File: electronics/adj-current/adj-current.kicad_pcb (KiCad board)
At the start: 2 copper layers, 9 parts, among them J1 Power, J2 Output, Q1 IRLZ44N, U1 LM358, U2 TL431DBZ

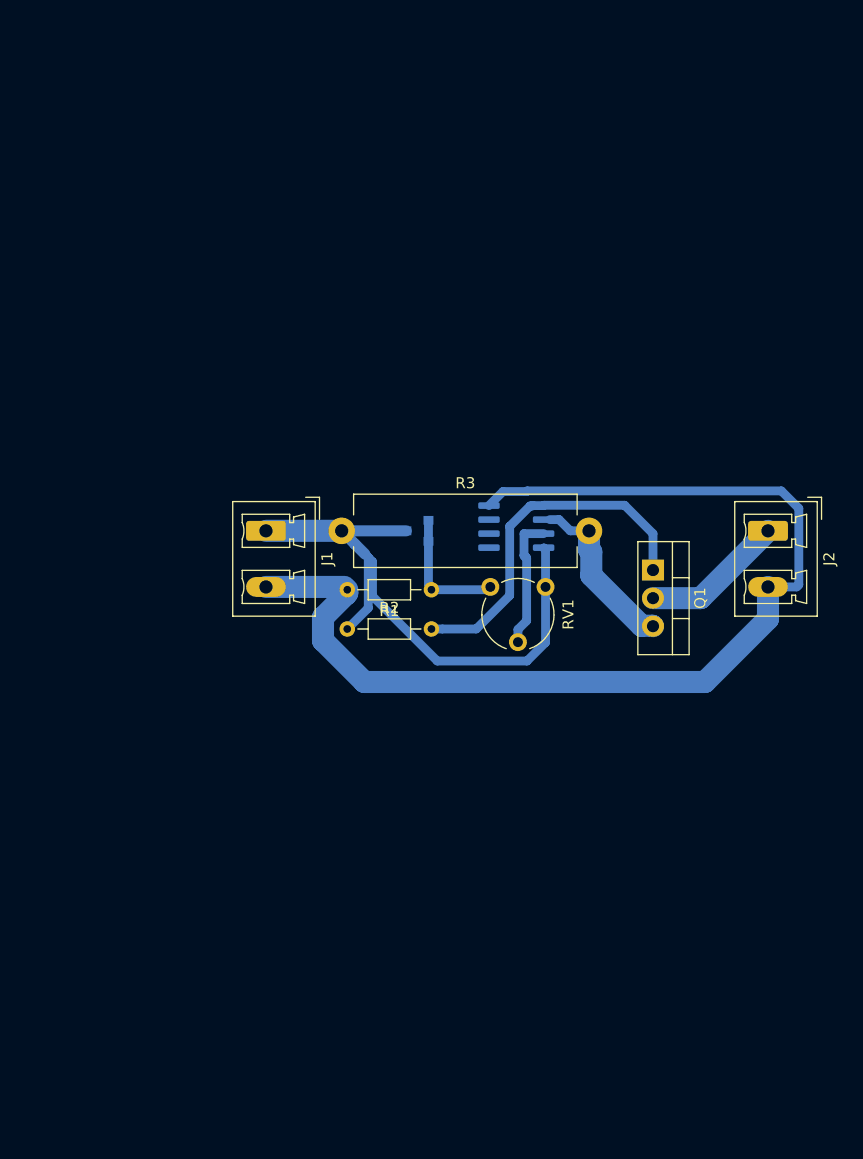
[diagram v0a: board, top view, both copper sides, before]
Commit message: adj current driver
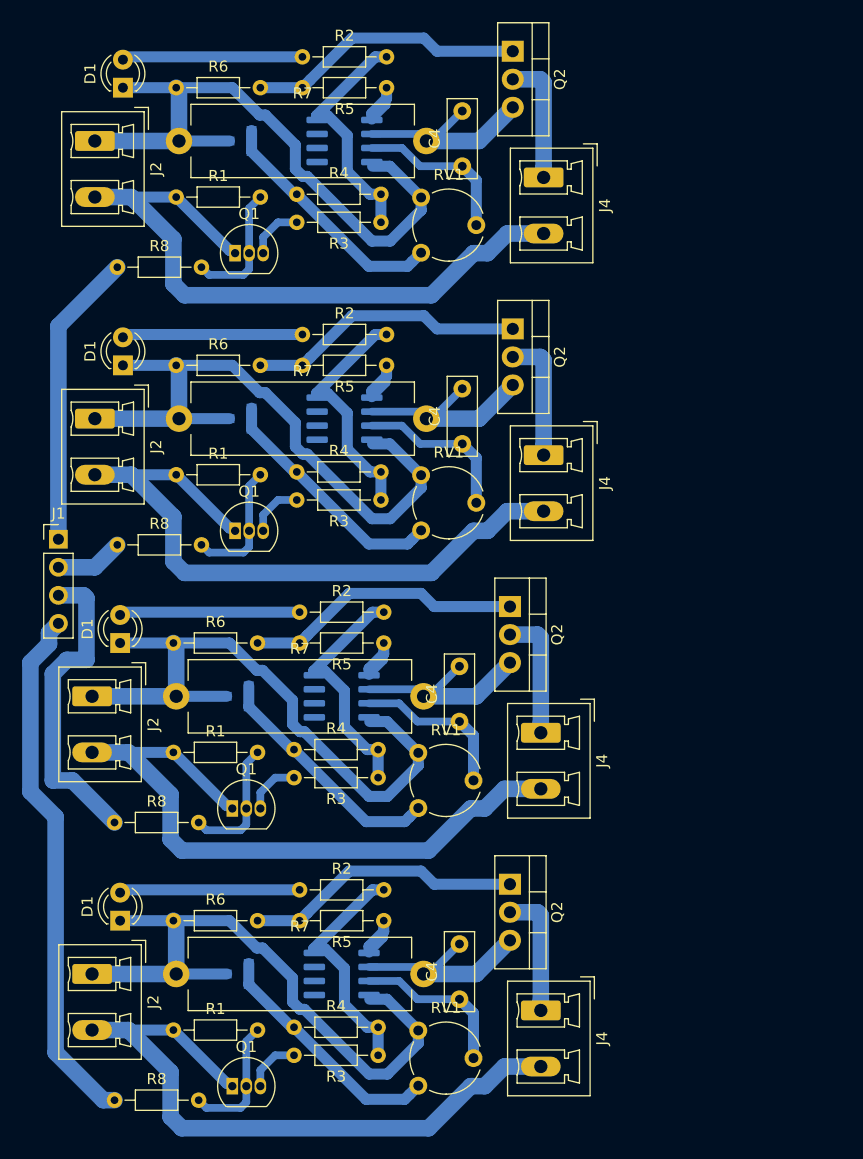
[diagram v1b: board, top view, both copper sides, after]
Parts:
- removed the J2 at (125.7, 72.4)
- removed the Q1 at (115.3, 75.9)
- removed the R1 at (95.2, 77.7)
- removed the R2 at (87.6, 81.3)
- removed the R3 at (87.1, 72.4)
- removed the RV1 at (100.6, 77.5)
- removed U1: LM358, Package_SO:SOIC-8_3.9x4.9mm_P1.27mm
- removed the U2 at (94.0, 72.4)
- added C4: 104, Capacitor_THT:C_Disc_D7.0mm_W2.5mm_P5.00mm, F.Cu at (97.8, 114.8)
- added C4: 104, Capacitor_THT:C_Disc_D7.0mm_W2.5mm_P5.00mm, F.Cu at (97.8, 89.7)
- added C4: 104, Capacitor_THT:C_Disc_D7.0mm_W2.5mm_P5.00mm, F.Cu at (98.0, 64.5)
- added C4: 104, Capacitor_THT:C_Disc_D7.0mm_W2.5mm_P5.00mm, F.Cu at (98.0, 39.4)
- added D1: LED, LED_THT:LED_D3.0mm, F.Cu at (67.1, 107.7)
- added D1: LED, LED_THT:LED_D3.0mm, F.Cu at (67.1, 82.5)
- added D1: LED, LED_THT:LED_D3.0mm, F.Cu at (67.3, 57.4)
- added D1: LED, LED_THT:LED_D3.0mm, F.Cu at (67.3, 32.3)
- added J2: Power, Connector_Phoenix_MC_HighVoltage:PhoenixContact_MCV_1,5_2-G-5.08_1x02_P5.08mm_Vertical, F.Cu at (64.5, 112.5)
- added J2: Power, Connector_Phoenix_MC_HighVoltage:PhoenixContact_MCV_1,5_2-G-5.08_1x02_P5.08mm_Vertical, F.Cu at (64.5, 87.4)
- added J2: Power, Connector_Phoenix_MC_HighVoltage:PhoenixContact_MCV_1,5_2-G-5.08_1x02_P5.08mm_Vertical, F.Cu at (64.8, 62.2)
- added J2: Power, Connector_Phoenix_MC_HighVoltage:PhoenixContact_MCV_1,5_2-G-5.08_1x02_P5.08mm_Vertical, F.Cu at (64.8, 37.1)
- added J4: Output, Connector_Phoenix_MC_HighVoltage:PhoenixContact_MCV_1,5_2-G-5.08_1x02_P5.08mm_Vertical, F.Cu at (105.2, 115.8)
- added J4: Output, Connector_Phoenix_MC_HighVoltage:PhoenixContact_MCV_1,5_2-G-5.08_1x02_P5.08mm_Vertical, F.Cu at (105.2, 90.7)
- added J4: Output, Connector_Phoenix_MC_HighVoltage:PhoenixContact_MCV_1,5_2-G-5.08_1x02_P5.08mm_Vertical, F.Cu at (105.4, 65.5)
- added J4: Output, Connector_Phoenix_MC_HighVoltage:PhoenixContact_MCV_1,5_2-G-5.08_1x02_P5.08mm_Vertical, F.Cu at (105.4, 40.4)
- added Q1: 2N3906, Package_TO_SOT_THT:TO-92_Inline, F.Cu at (77.2, 122.7)
- added Q1: 2N3906, Package_TO_SOT_THT:TO-92_Inline, F.Cu at (77.2, 97.5)
- added Q1: 2N3906, Package_TO_SOT_THT:TO-92_Inline, F.Cu at (77.5, 72.4)
- added Q1: 2N3906, Package_TO_SOT_THT:TO-92_Inline, F.Cu at (77.5, 47.2)
- added Q2: IRLZ44N, Package_TO_SOT_THT:TO-220-3_Vertical, F.Cu at (102.4, 104.4)
- added Q2: IRLZ44N, Package_TO_SOT_THT:TO-220-3_Vertical, F.Cu at (102.4, 79.2)
- added Q2: IRLZ44N, Package_TO_SOT_THT:TO-220-3_Vertical, F.Cu at (102.6, 54.1)
- added Q2: IRLZ44N, Package_TO_SOT_THT:TO-220-3_Vertical, F.Cu at (102.6, 29.0)
- added R1: 10k, Resistor_THT:R_Axial_DIN0204_L3.6mm_D1.6mm_P7.62mm_Horizontal, F.Cu at (71.9, 117.6)
- added R1: 10k, Resistor_THT:R_Axial_DIN0204_L3.6mm_D1.6mm_P7.62mm_Horizontal, F.Cu at (71.9, 92.5)
- added R1: 10k, Resistor_THT:R_Axial_DIN0204_L3.6mm_D1.6mm_P7.62mm_Horizontal, F.Cu at (72.1, 67.3)
- added R1: 10k, Resistor_THT:R_Axial_DIN0204_L3.6mm_D1.6mm_P7.62mm_Horizontal, F.Cu at (72.1, 42.2)
- added R2: 1k, Resistor_THT:R_Axial_DIN0204_L3.6mm_D1.6mm_P7.62mm_Horizontal, F.Cu at (83.3, 104.9)
- added R2: 1k, Resistor_THT:R_Axial_DIN0204_L3.6mm_D1.6mm_P7.62mm_Horizontal, F.Cu at (83.3, 79.8)
- added R2: 1k, Resistor_THT:R_Axial_DIN0204_L3.6mm_D1.6mm_P7.62mm_Horizontal, F.Cu at (83.6, 54.6)
- added R2: 1k, Resistor_THT:R_Axial_DIN0204_L3.6mm_D1.6mm_P7.62mm_Horizontal, F.Cu at (83.6, 29.5)
- added R3: 470, Resistor_THT:R_Axial_DIN0204_L3.6mm_D1.6mm_P7.62mm_Horizontal, F.Cu at (90.4, 119.9)
- added R3: 470, Resistor_THT:R_Axial_DIN0204_L3.6mm_D1.6mm_P7.62mm_Horizontal, F.Cu at (90.4, 94.7)
- added R3: 470, Resistor_THT:R_Axial_DIN0204_L3.6mm_D1.6mm_P7.62mm_Horizontal, F.Cu at (90.7, 69.6)
- added R3: 470, Resistor_THT:R_Axial_DIN0204_L3.6mm_D1.6mm_P7.62mm_Horizontal, F.Cu at (90.7, 44.5)
- added R4: 1.7k, Resistor_THT:R_Axial_DIN0204_L3.6mm_D1.6mm_P7.62mm_Horizontal, F.Cu at (82.8, 117.3)
- added R4: 1.7k, Resistor_THT:R_Axial_DIN0204_L3.6mm_D1.6mm_P7.62mm_Horizontal, F.Cu at (82.8, 92.2)
- added R4: 1.7k, Resistor_THT:R_Axial_DIN0204_L3.6mm_D1.6mm_P7.62mm_Horizontal, F.Cu at (83.1, 67.1)
- added R4: 1.7k, Resistor_THT:R_Axial_DIN0204_L3.6mm_D1.6mm_P7.62mm_Horizontal, F.Cu at (83.1, 41.9)
- added R5: 100, Resistor_THT:R_Axial_DIN0204_L3.6mm_D1.6mm_P7.62mm_Horizontal, F.Cu at (90.9, 107.7)
- added R5: 100, Resistor_THT:R_Axial_DIN0204_L3.6mm_D1.6mm_P7.62mm_Horizontal, F.Cu at (90.9, 82.5)
- added R5: 100, Resistor_THT:R_Axial_DIN0204_L3.6mm_D1.6mm_P7.62mm_Horizontal, F.Cu at (91.2, 57.4)
- added R5: 100, Resistor_THT:R_Axial_DIN0204_L3.6mm_D1.6mm_P7.62mm_Horizontal, F.Cu at (91.2, 32.3)
- added R6: 1k, Resistor_THT:R_Axial_DIN0204_L3.6mm_D1.6mm_P7.62mm_Horizontal, F.Cu at (71.9, 107.7)
- added R6: 1k, Resistor_THT:R_Axial_DIN0204_L3.6mm_D1.6mm_P7.62mm_Horizontal, F.Cu at (71.9, 82.5)
- added R6: 1k, Resistor_THT:R_Axial_DIN0204_L3.6mm_D1.6mm_P7.62mm_Horizontal, F.Cu at (72.1, 57.4)
- added R6: 1k, Resistor_THT:R_Axial_DIN0204_L3.6mm_D1.6mm_P7.62mm_Horizontal, F.Cu at (72.1, 32.3)
- added R7: 2, Resistor_THT:R_Axial_Power_L20.0mm_W6.4mm_P22.40mm, F.Cu at (72.1, 112.5)
- added R7: 2, Resistor_THT:R_Axial_Power_L20.0mm_W6.4mm_P22.40mm, F.Cu at (72.1, 87.4)
- added R7: 2, Resistor_THT:R_Axial_Power_L20.0mm_W6.4mm_P22.40mm, F.Cu at (72.4, 62.2)
- added R7: 2, Resistor_THT:R_Axial_Power_L20.0mm_W6.4mm_P22.40mm, F.Cu at (72.4, 37.1)
- added R8: 1k, Resistor_THT:R_Axial_DIN0204_L3.6mm_D1.6mm_P7.62mm_Horizontal, F.Cu at (66.5, 124.0)
- added R8: 1k, Resistor_THT:R_Axial_DIN0204_L3.6mm_D1.6mm_P7.62mm_Horizontal, F.Cu at (66.5, 98.8)
- added R8: 1k, Resistor_THT:R_Axial_DIN0204_L3.6mm_D1.6mm_P7.62mm_Horizontal, F.Cu at (66.8, 73.7)
- added R8: 1k, Resistor_THT:R_Axial_DIN0204_L3.6mm_D1.6mm_P7.62mm_Horizontal, F.Cu at (66.8, 48.5)
- added RV1: R_POT, Potentiometer_THT:Potentiometer_Piher_PT-6-V_Vertical, F.Cu at (94.1, 122.6)
- added RV1: R_POT, Potentiometer_THT:Potentiometer_Piher_PT-6-V_Vertical, F.Cu at (94.1, 97.5)
- added RV1: R_POT, Potentiometer_THT:Potentiometer_Piher_PT-6-V_Vertical, F.Cu at (94.3, 72.3)
- added RV1: R_POT, Potentiometer_THT:Potentiometer_Piher_PT-6-V_Vertical, F.Cu at (94.3, 47.2)
- added U2: LM358, Package_SO:SOIC-8_3.9x4.9mm_P1.27mm, B.Cu at (87.1, 112.5)
- added U2: LM358, Package_SO:SOIC-8_3.9x4.9mm_P1.27mm, B.Cu at (87.1, 87.4)
- added U2: LM358, Package_SO:SOIC-8_3.9x4.9mm_P1.27mm, B.Cu at (87.4, 62.2)
- added U2: LM358, Package_SO:SOIC-8_3.9x4.9mm_P1.27mm, B.Cu at (87.4, 37.1)
- added U3: TL431DBZ, Package_TO_SOT_SMD:SOT-23, B.Cu at (77.7, 112.5)
- added U3: TL431DBZ, Package_TO_SOT_SMD:SOT-23, B.Cu at (77.7, 87.4)
- added U3: TL431DBZ, Package_TO_SOT_SMD:SOT-23, B.Cu at (78.0, 62.2)
- added U3: TL431DBZ, Package_TO_SOT_SMD:SOT-23, B.Cu at (78.0, 37.1)
- J1: value Power -> Controls; footprint Connector_Phoenix_MC_HighVoltage:PhoenixContact_MCV_1,5_2-G-5.08_1x02_P5.08mm_Vertical -> Connector_PinHeader_2.54mm:PinHeader_1x04_P2.54mm_Vertical
- moved J1 18.8 mm to (61.5, 73.2), turned to 0 degrees
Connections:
- J1 pad 1: GND -> Net-(J1-Pad1)
- J1 pad 2: Net-(J1-Pad2) -> (no net)
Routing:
- net (no net): track 0.00 -> 913.7 mm
- net Net-(J1-Pad2): track 108.9 -> 0.00 mm
- net vss: track 0.00 -> 63.9 mm
- net Net-(Q1-Pad1): track 32.7 -> 0.00 mm
- net Net-(J1-Pad1): track 0.00 -> 26.8 mm
- net Net-(Q2-Pad1): track 0.00 -> 25.2 mm
- net Net-(R4-Pad1): track 0.00 -> 22.1 mm
- net Net-(R2-Pad2): track 0.00 -> 21.8 mm
- net Net-(C4-Pad2): track 0.00 -> 18.7 mm
- net Net-(D1-Pad2): track 0.00 -> 16.4 mm
- net Net-(C4-Pad1): track 0.00 -> 14.7 mm
- net Net-(J2-Pad1): track 12.9 -> 0.00 mm
- net Net-(RV1-Pad2): track 12.4 -> 0.00 mm
- net Net-(R1-Pad1): track 11.8 -> 0.00 mm
- net A_ctrl: track 0.00 -> 11.8 mm
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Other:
- net class Default: trace_width 0.8 -> 1.5; via_dia 1.5 -> 1
